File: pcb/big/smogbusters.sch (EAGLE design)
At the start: 22 parts, among them Q1 IRLZ44N

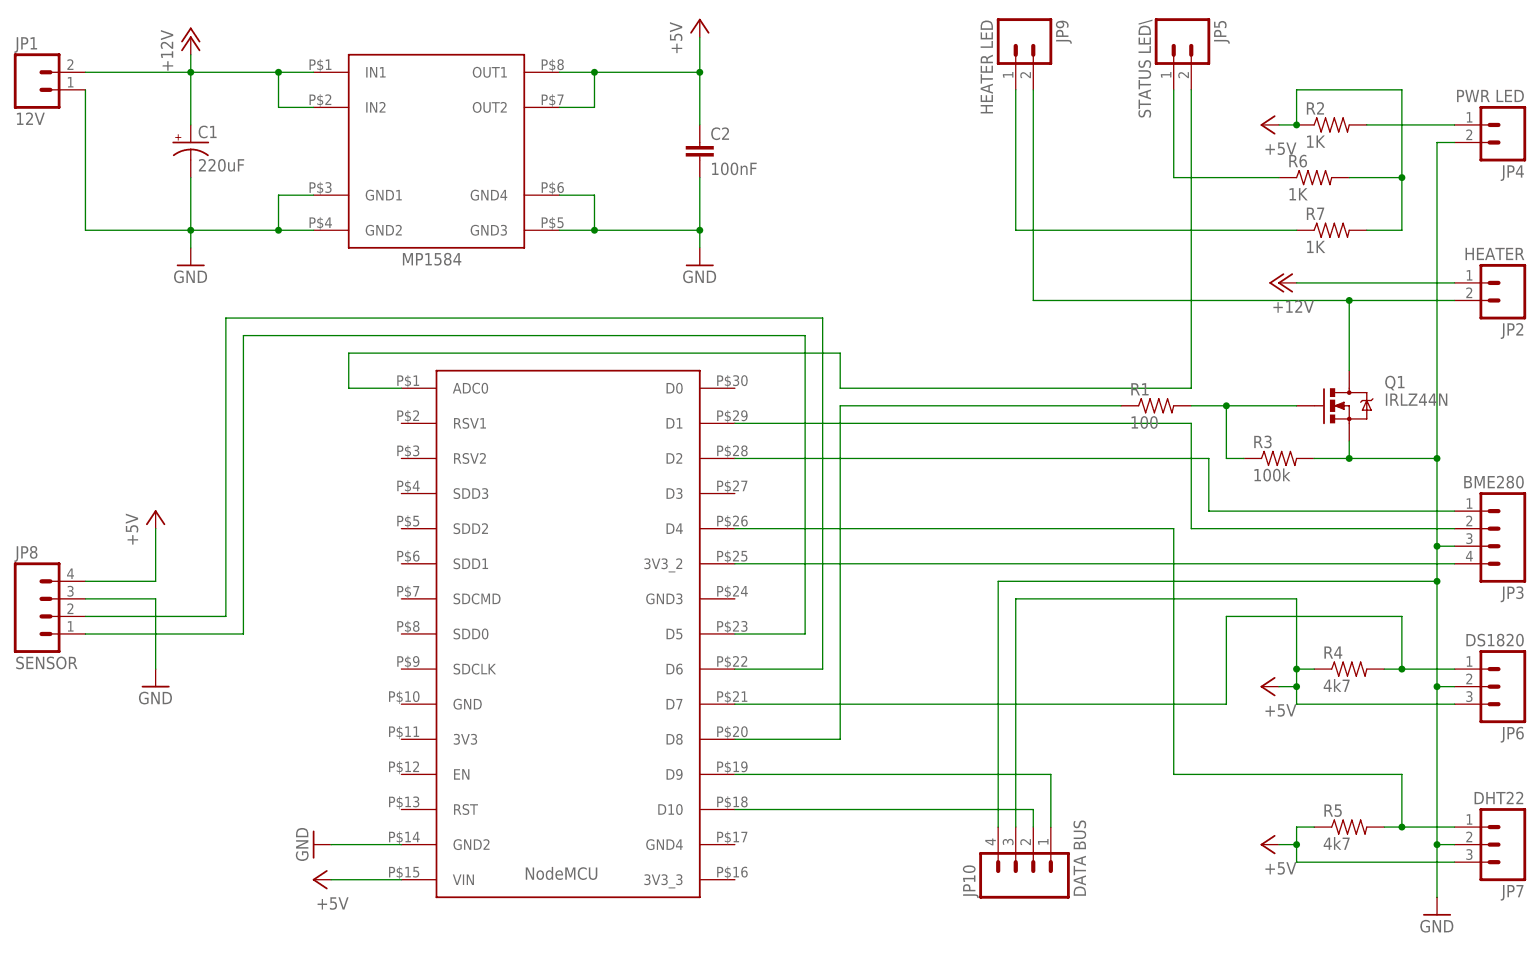
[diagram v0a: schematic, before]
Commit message: PCB fixes acc. to ticket #1
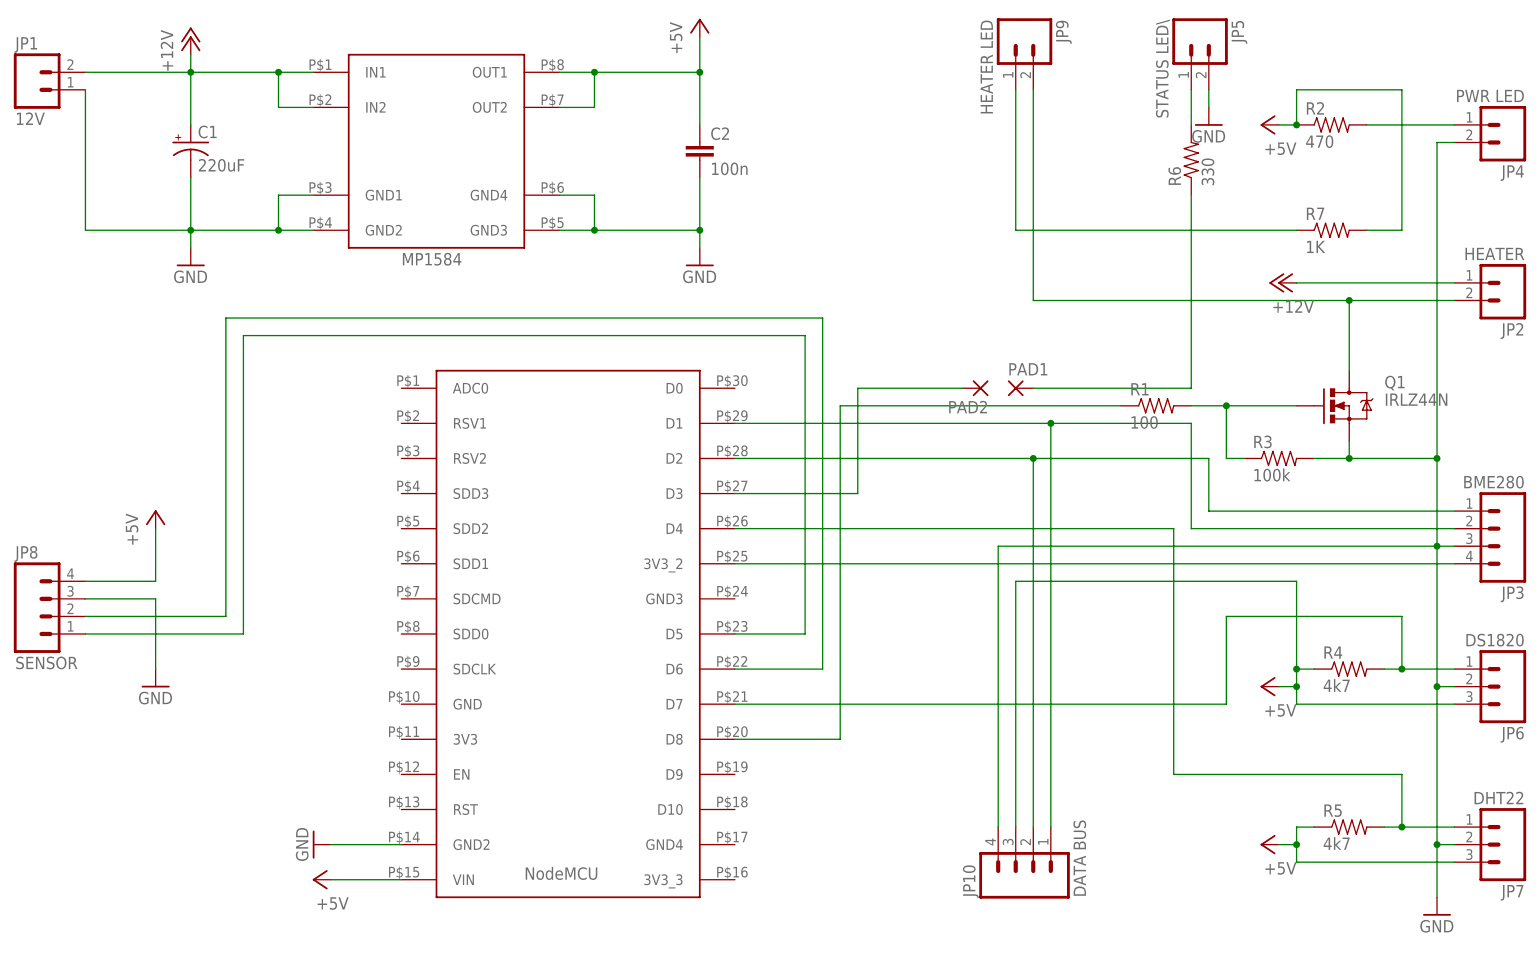
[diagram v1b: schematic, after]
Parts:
- added PAD1, PAD2: (no value), wirepad:1,6/0,8
- C2: value 100nF -> 100n; device SparkFun-Capacitors:CAPPTH1 -> capacitor-wima:C5/2.5
- R2: value 1K -> 470
- R6: value 1K -> 330
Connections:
- removed net N$10: JP3.1, U$1.D2
- removed net N$11: JP3.2, U$1.D1
- new net N$4: JP5.1, R6.2
- net +5V: no longer R6.2
- net GND: now also JP5.2
- net N$12: now also PAD1.P; no longer JP5.1
- net N$14: now also PAD2.P, U$1.D3; no longer JP5.2, U$1.ADC0
- net N$16: now also JP10.2, JP3.1, U$1.D2; no longer JP10.1, U$1.D9
- net N$17: now also JP10.1, JP3.2, U$1.D1; no longer JP10.2, U$1.D10
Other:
- moved on the sheet: JP5, R6
